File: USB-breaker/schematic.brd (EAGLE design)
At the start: 67.5 x 45.5 mm, 19 parts, among them K1 G6K-2P, K3 G6K-2P, T1 BC558B, T2 BC548B, X1 PN61729-S, X2 PN87520-S, X3 10104110, X4 UX60SC-MB-5ST

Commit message: First parts placed
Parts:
- added H1, H2, H3, H4: MOUNT-PAD-ROUND3.0, holes:3,0-PAD
- moved X3 105.4 mm to (66.0, 35.6), turned to 90 degrees
- moved X4 89.5 mm to (67.3, 10.2), turned to 90 degrees
- moved X1 82.1 mm to (58.4, 22.8), turned to 90 degrees
- moved K1 76.5 mm to (38.1, 36.8)
- moved K3 76.5 mm to (27.9, 36.8)
- moved R2 62.0 mm to (6.35, 69.8)
- moved JP1 61.9 mm to (21.6, 7.62), turned to 180 degrees
- moved X2 52.0 mm to (8.89, 22.8), turned to 270 degrees
- moved T2 40.7 mm to (14.0, 50.8)
- moved SV1 36.1 mm to (6.35, 63.5)
- moved T1 22.9 mm to (5.08, 52.1)

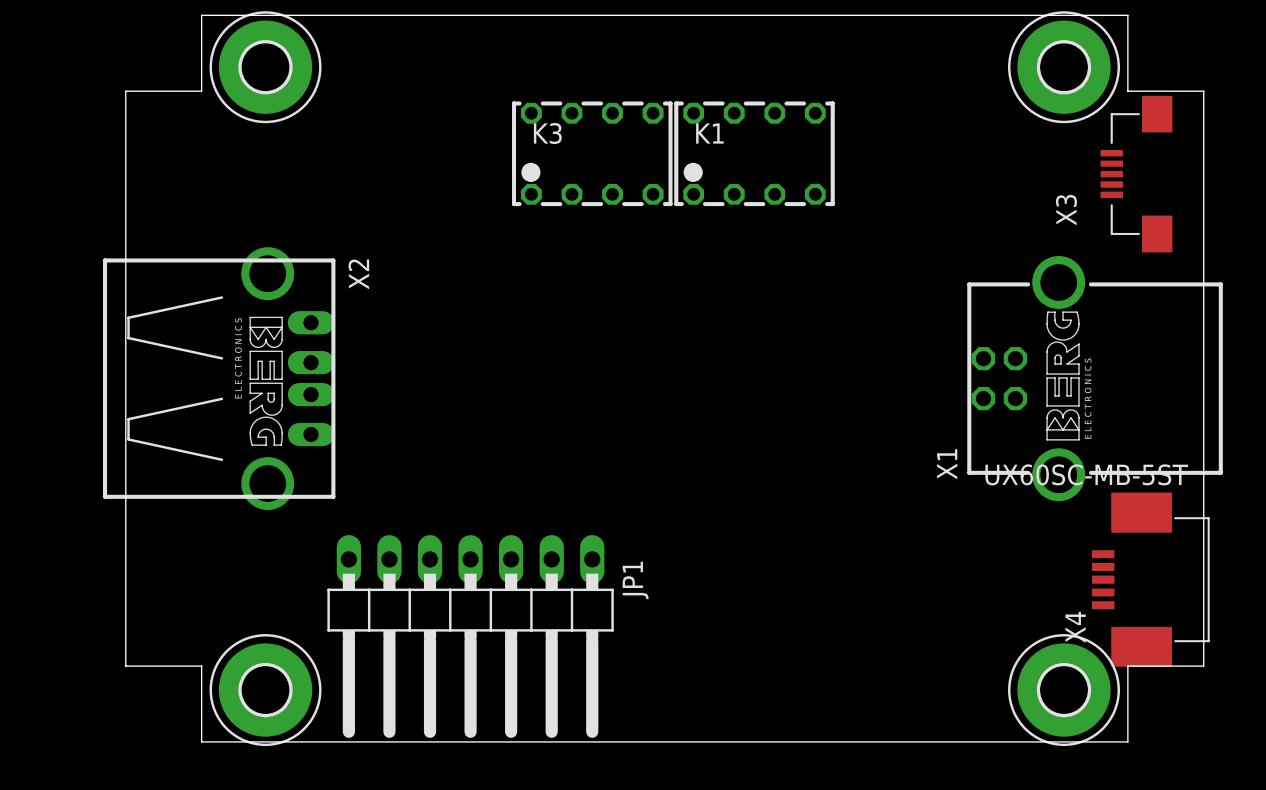
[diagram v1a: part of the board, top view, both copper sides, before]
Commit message: The four USB connectors should be properly placed now.
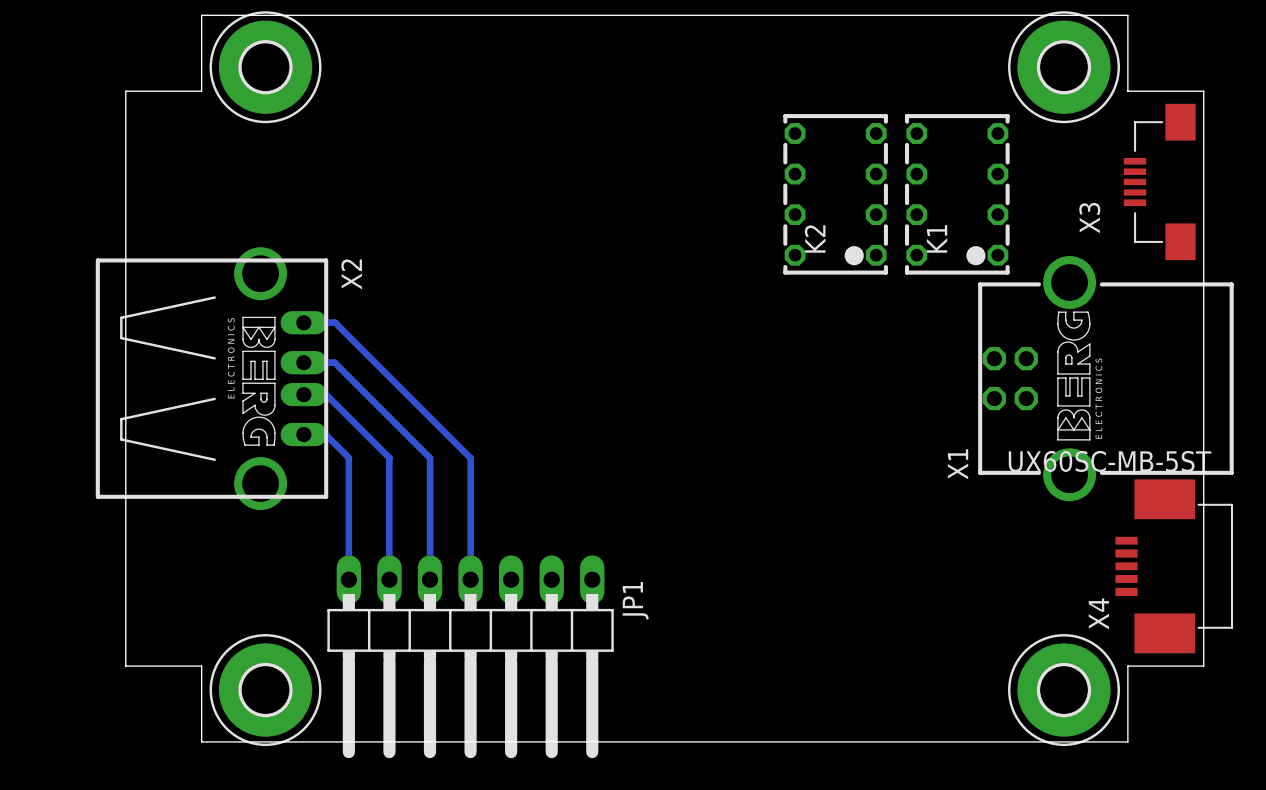
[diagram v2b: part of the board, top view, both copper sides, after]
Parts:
- removed K3: G6K-2P, relay:G6K-2P
- added K2: G6K-2P, relay:G6K-2P
- moved K1 14.5 mm to (52.1, 33.0), turned to 90 degrees
- moved X4 1.68 mm to (68.8, 11.0)
- moved X3 1.54 mm to (67.5, 35.1)
- moved JP1 1.27 mm to (21.6, 6.35)
- moved X1 0.68 mm to (59.1, 22.8)
- moved X2 0.45 mm to (8.44, 22.8)
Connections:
- net ENABLE: now also K2.1; no longer K3.1
- net GND_IN: now also K2.3, K2.8; no longer K3.3, K3.8
- net GND_OUT: now also K2.2; no longer K3.2
- net VCC_IN: now also K2.6; no longer K3.6
- net VCC_LED: now also K2.5; no longer K3.5
- net VCC_OUT: now also K2.7; no longer K3.7
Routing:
- net VCC_OUT: track 0.00 -> 21.6 mm
- net D-_OUT: track 0.00 -> 18.0 mm
- net D+_OUT: track 0.00 -> 14.6 mm
- net GND_OUT: track 0.00 -> 11.0 mm

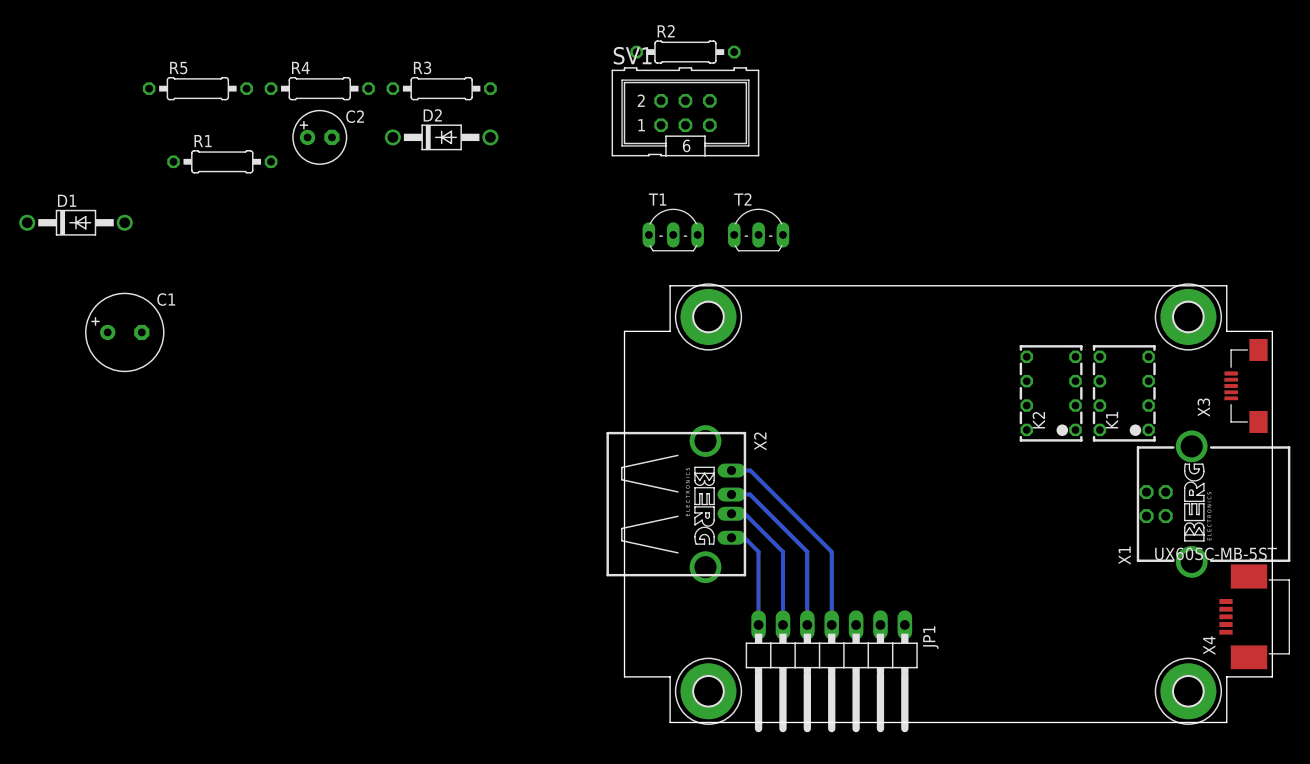
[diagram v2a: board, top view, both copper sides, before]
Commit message: The mechanical design should be good now. Also started placing the components on the board.
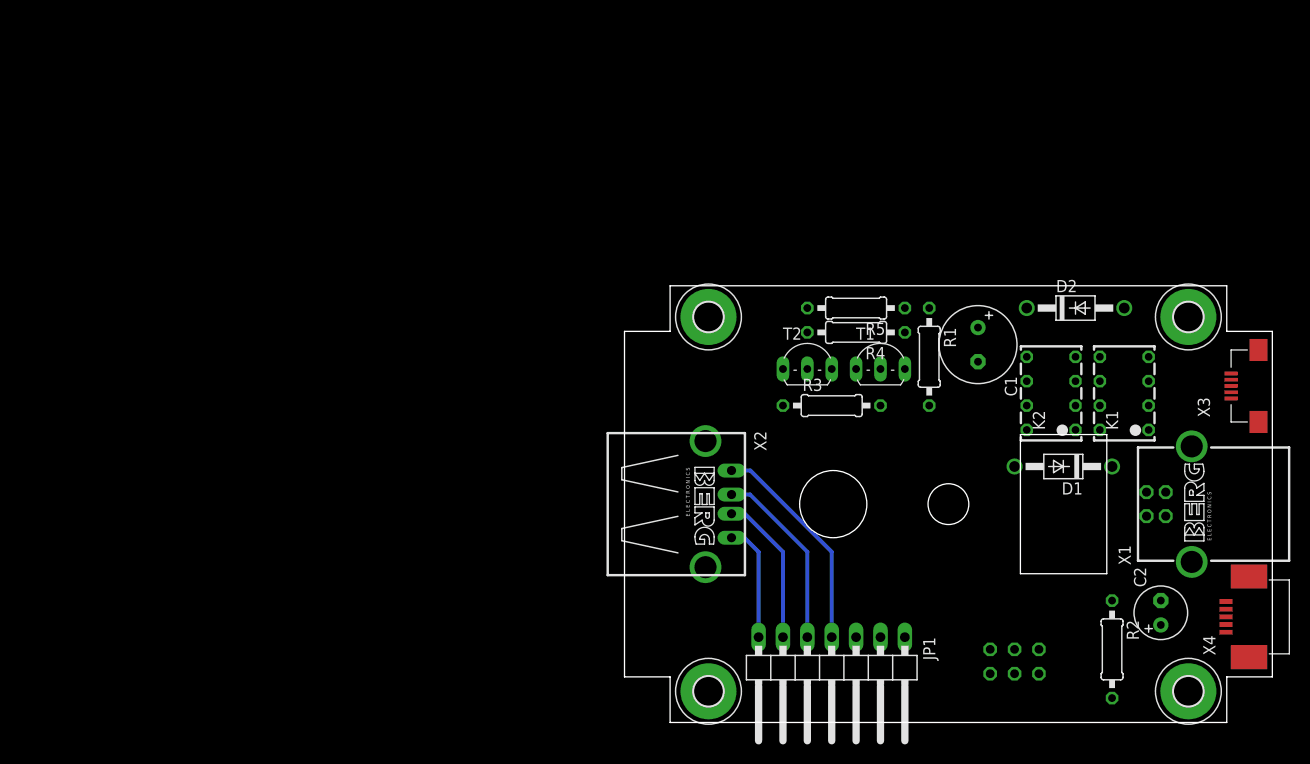
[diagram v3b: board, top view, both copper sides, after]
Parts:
- moved D1 106.0 mm to (45.7, 26.7), turned to 180 degrees
- moved C2 100.7 mm to (55.9, 11.4), turned to 90 degrees
- moved C1 88.9 mm to (36.8, 39.4), turned to 270 degrees
- moved R2 76.5 mm to (50.8, 7.62), turned to 270 degrees
- moved R1 76.4 mm to (31.8, 38.1), turned to 270 degrees
- moved R5 72.3 mm to (24.1, 43.2), turned to 180 degrees
- moved D2 68.4 mm to (47.0, 43.2)
- moved SV1 66.6 mm to (40.6, 6.35), flipped to the bottom
- moved R4 61.4 mm to (24.1, 40.6), turned to 180 degrees
- moved R3 52.4 mm to (21.6, 33.0)
- moved T1 25.7 mm to (26.7, 38.1)
- moved T2 14.9 mm to (19.1, 36.8)
- moved JP1 1.27 mm to (21.6, 5.08)
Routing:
- net VCC_OUT: track 21.6 -> 22.8 mm
- net GND_OUT: track 11.0 -> 12.3 mm
- net D-_OUT: track 18.0 -> 19.3 mm
- net D+_OUT: track 14.6 -> 15.9 mm
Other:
- outline, holes or cut-outs redrawn

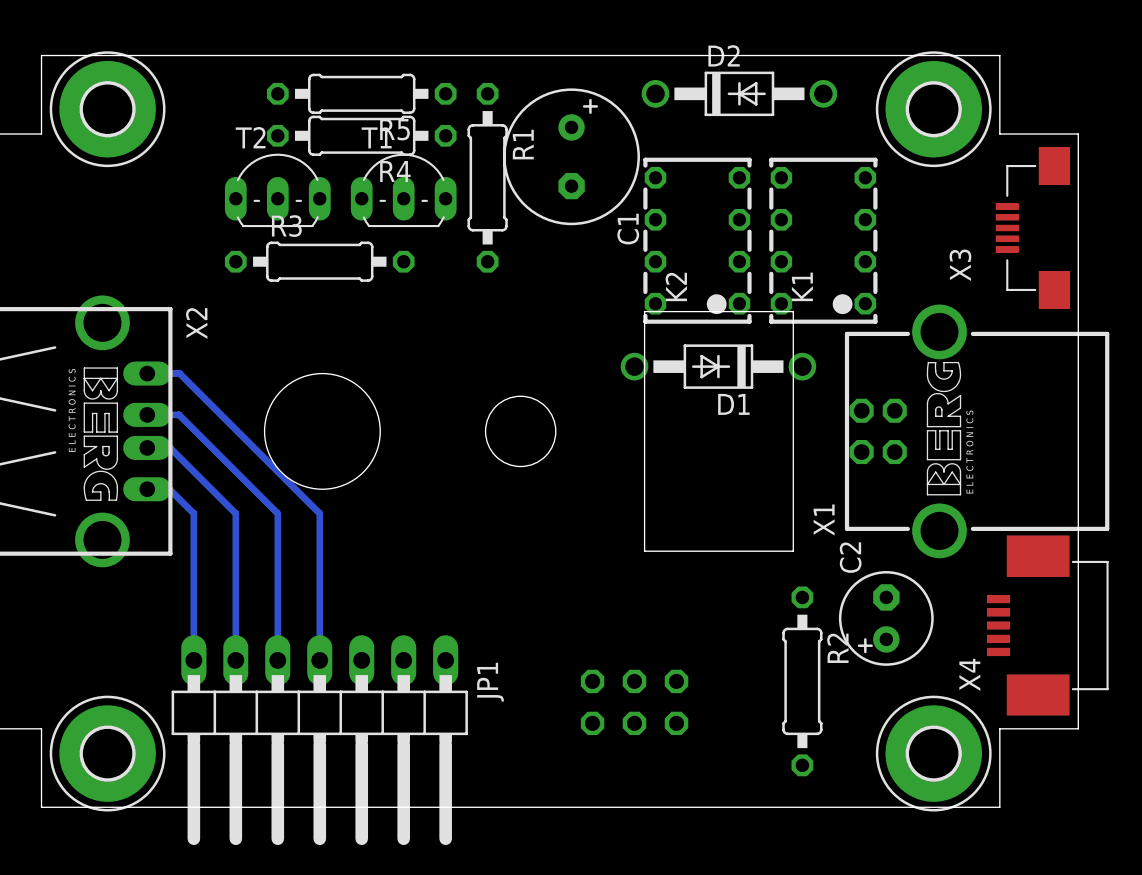
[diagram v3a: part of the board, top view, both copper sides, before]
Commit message: PCB layout, part one
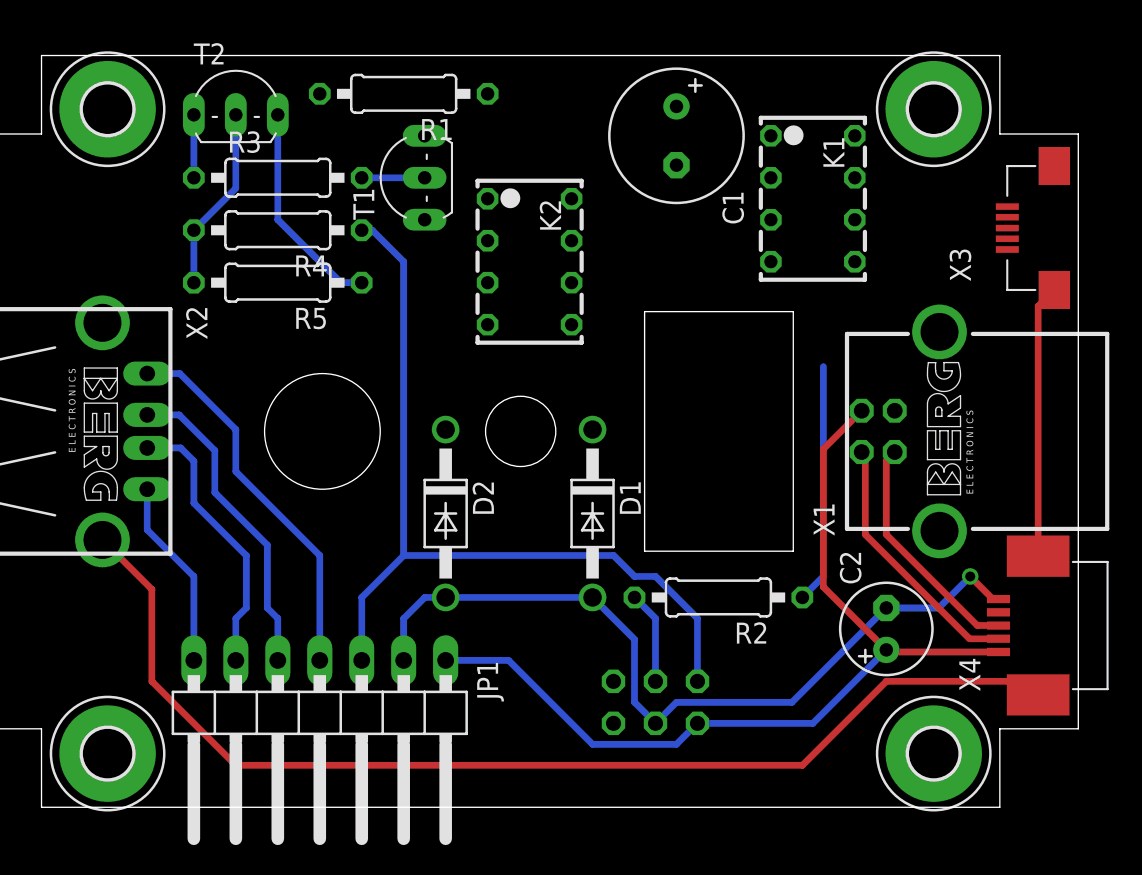
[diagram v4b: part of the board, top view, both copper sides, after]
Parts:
- moved D2 31.0 mm to (29.2, 17.8), turned to 270 degrees
- moved R5 12.5 mm to (19.1, 31.8)
- moved D1 11.7 mm to (38.1, 17.8), turned to 270 degrees
- moved K2 10.2 mm to (34.3, 34.3), turned to 270 degrees
- moved R4 7.65 mm to (19.1, 34.9)
- moved R1 7.18 mm to (26.7, 43.2), turned to 180 degrees
- moved R2 7.18 mm to (45.7, 12.7), turned to 180 degrees
- moved C1 6.48 mm to (43.2, 40.6)
- moved R3 5.68 mm to (19.1, 38.1)
- moved T2 5.68 mm to (16.5, 41.9)
- moved K1 5.12 mm to (51.4, 38.1), turned to 270 degrees
- moved SV1 1.27 mm to (41.9, 6.35)
- moved C2 0.63 mm to (55.9, 10.8)
- turned T1 to 90 degrees
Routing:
- net SHIELD: track 0.00 -> 84.5 mm
- net GND_IN: track 0.00 -> 61.7 mm, vias 0 -> 1
- net VCC_IN: track 0.00 -> 55.0 mm
- net EXTERNAL_ENABLE: track 0.00 -> 51.7 mm
- net D-_IN: track 0.00 -> 15.8 mm
- net VCC_LED: track 0.00 -> 14.5 mm
- net D+_IN: track 0.00 -> 14.3 mm
- net N$3: track 0.00 -> 11.2 mm
- net LED: track 0.00 -> 5.61 mm
- net N$1: track 0.00 -> 3.81 mm
- net N$2: track 0.00 -> 3.81 mm
- net GND_OUT: track 12.3 -> 11.5 mm
- net D+_OUT: track 15.9 -> 16.7 mm

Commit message: PCB layout, part two
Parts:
- moved D1 27.4 mm to (48.3, 43.2), turned to 0 degrees
- moved D2 21.9 mm to (33.0, 39.4), turned to 0 degrees
- moved R1 8.89 mm to (35.6, 43.2)
- moved K2 4.02 mm to (33.0, 30.5), turned to 90 degrees
- moved C1 3.81 mm to (43.2, 36.8)
- moved T1 3.59 mm to (24.1, 40.6), turned to 180 degrees
- moved K1 1.27 mm to (51.4, 36.8)
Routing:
- net GND_IN: track 61.7 -> 111.4 mm
- net D-_IN: track 15.8 -> 51.6 mm
- net D+_IN: track 14.3 -> 45.0 mm
- net VCC_IN: track 55.0 -> 70.2 mm
- net N$8: track 0.00 -> 13.1 mm
- net D+_OUT: track 16.7 -> 29.8 mm
- net EXTERNAL_ENABLE: track 51.7 -> 39.0 mm
- net D-_OUT: track 19.3 -> 26.8 mm
- net SHIELD: track 84.5 -> 91.1 mm

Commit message: PCB layout, part three
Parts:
- moved R2 18.1 mm to (28.6, 18.4), turned to 270 degrees
- moved K2 2.84 mm to (31.8, 33.0), turned to 270 degrees
- moved D2 1.42 mm to (34.3, 40.0)
- moved R1 1.27 mm to (34.3, 43.2)
- moved C1 0.63 mm to (43.2, 36.2)
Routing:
- net VCC_IN: track 70.2 -> 133.8 mm
- net D+_OUT: track 29.8 -> 74.4 mm
- net D-_OUT: track 26.8 -> 71.2 mm
- net GND_OUT: track 11.5 -> 55.5 mm
- net GND_IN: track 111.4 -> 153.8 mm
- net VCC_OUT: track 22.8 -> 50.3 mm
- net ENABLE: track 0.00 -> 17.6 mm
- net LED: track 5.61 -> 15.7 mm
- net EXTERNAL_ENABLE: track 39.0 -> 49.1 mm
- net VCC_LED: track 14.5 -> 8.30 mm
- net N$8: track 13.1 -> 15.3 mm
- net SHIELD: track 91.1 -> 92.2 mm
